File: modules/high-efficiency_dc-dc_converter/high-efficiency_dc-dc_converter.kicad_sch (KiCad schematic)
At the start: 13 parts

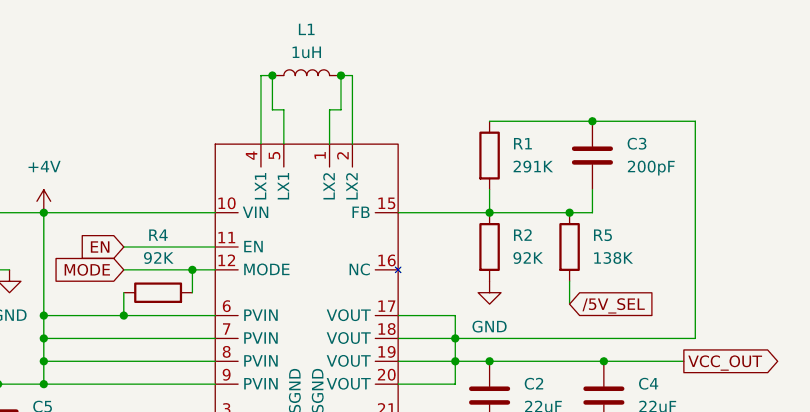
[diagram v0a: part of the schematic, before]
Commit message: Adding more mouser parts to schematics
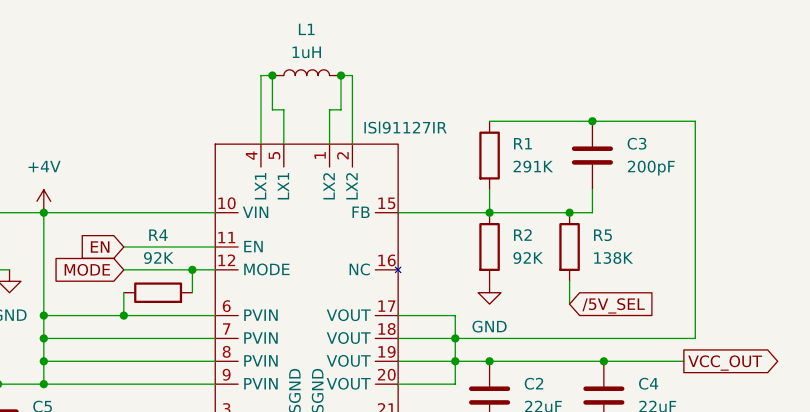
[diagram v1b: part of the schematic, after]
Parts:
- R2, R4: Mft. PN (none) -> RN73H1JTTD9202B25; Mouser (none) -> https://eu.mouser.com/ProductDetail/KOA-Speer/RN73H1JTTD920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; Mouser PN (none) -> 660-RN73H1JTD9202B25
- U1: value ~ -> ISl91127IR; Mft. PN (none) -> ISL91127IRAZ-T7A; Mouser (none) -> https://eu.mouser.com/ProductDetail/Renesas-Intersil/ISL911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; Mouser PN (none) -> 968-ISL91127IRAZ-T

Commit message: Updating parts
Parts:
- C1, C5: DigiKey (none) -> https://www.digikey.com.au/en/products/detail/samsung-elect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; Mft. PN (none) -> CL21A106KOQNNNG; Mouser (none) -> https://hr.mouser.com/ProductDetail/Samsung-Electro-Mechani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; Mouser PN (none) -> 187-CL21A106KOQNNNG
- C2, C4: DigiKey (none) -> https://www.digikey.com.au/en/products/detail/samsung-elect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; Mft. PN (none) -> CL21A226KOQNNNG; Mouser (none) -> https://hr.mouser.com/ProductDetail/Samsung-Electro-Mechani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; Mouser PN (none) -> 187-CL21A226KOQNNNG
- C3: DigiKey (none) -> https://www.digikey.com.au/en/products/detail/yageo/CC0805J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; Mft. PN (none) -> CC0805JRNPO9BN201; Mouser (none) -> 603-CC805JRNPO9BN201; Mouser PN (none) -> https://hr.mouser.com/ProductDetail/YAGEO/CC0805JRNPO9BN201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
- L1: DigiKey (none) -> https://www.digikey.com.au/en/products/detail/koa-speer-ele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; Mft. PN (none) -> DFE252012P-1R0M=P2; Mouser (none) -> https://hr.mouser.com/ProductDetail/Murata-Electronics/DFE2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; Mouser PN (none) -> 81-DFE252012P-1R0MP2
- R1: DigiKey (none) -> https://www.digikey.com/en/products/detail/koa-speer-electr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; Mft. PN (none) -> RN73R1JTTD2913F100
- R2, R4: DigiKey (none) -> https://www.digikey.com.au/en/products/detail/yageo/RC0603F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; Mft. PN RN73H1JTTD9202B25 -> RC0603FR-0791KL; Mouser https://eu.mouser.com/ProductDetail/KOA-Speer/RN73H1JTTD920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 -> https://hr.mouser.com/ProductDetail/YAGEO/RC0603FR-0791KL?q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; Mouser PN 660-RN73H1JTD9202B25 -> 603-RC0603FR-0791KL
- R5: DigiKey (none) -> https://www.digikey.com.au/en/products/detail/koa-speer-ele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; Mft. PN (none) -> RK73H1JTTD1403F; Mouser (none) -> https://eu.mouser.com/ProductDetail/KOA-Speer/RK73H1JTTD140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; Mouser PN (none) -> 660-RK73H1JTTD1403F
- U1: DigiKey (none) -> https://www.digikey.com/en/products/detail/renesas-electron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
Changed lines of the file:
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@@
 			)
 		)
-		(property "Mft. PN" ""
+		(property "Mft. PN" "RK73H1JTTD1403F"
 			(at 101.6 62.23 0)
 			(effects
@@
 			)
 		)
-		(property "Mouser" ""
+		(property "Mouser" "https://eu.mouser.com/ProductDetail/KOA-Speer/RK73H1JTTD1403F?qs=XOvILOgadXaHJrsLzSCu9w%3D%3D"
 			(at 101.6 62.23 0)
 			(effects
@@
 			)
 		)
-		(property "Mouser PN" ""
+		(property "Mouser PN" "660-RK73H1JTTD1403F"
+			(at 101.6 62.23 0)
+			(effects
+				(font
+					(size 1.27 1.27)
+				)
+				(hide yes)
+			)
+		)
+		(property "DigiKey" "https://www.digikey.com.au/en/products/detail/koa-speer-electronics-inc/RK73H1JTTD1403F/9845164"
 			(at 101.6 62.23 0)
 			(effects
@@
 			)
 		)
-		(property "Mft. PN" ""
+		(property "Mft. PN" "RN73R1JTTD2913F100"
 			(at 92.71 52.07 0)
 			(effects
@@
 		)
 		(property "Mouser PN" ""
+			(at 92.71 52.07 0)
+			(effects
+				(font
+					(size 1.27 1.27)
+				)
+				(hide yes)
+			)
+		)
+		(property "DigiKey" "https://www.digikey.com/en/products/detail/koa-speer-electronics-inc/RN73R1JTTD2913F100/10014619?s=N4IgTCBcDaIEoDkDsBmOBGAUgFWwETAE50UAxdABgpAF0BfIA"
 			(at 92.71 52.07 0)
 			(effects
@@
 			)
 		)
+		(property "DigiKey" "https://www.digikey.com/en/products/detail/renesas-electronics-corporation/ISL91127IRAZ-T7A/6163917"
+			(at 72.39 67.31 0)
+			(effects
+				(font
+					(size 1.27 1.27)
+				)
+				(hide yes)
+			)
+		)
 		(pin "5"
 		)
@@
 			)
 		)
-		(property "Mft. PN" "RN73H1JTTD9202B25"
+		(property "Mft. PN" "RC0603FR-0791KL"
 			(at 92.71 62.23 0)
 			(effects
@@
 			)
 		)
-		(property "Mouser" "https://eu.mouser.com/ProductDetail/KOA-Speer/RN73H1JTTD9202B25?qs=pJKkPLTLvBhLL59WGnN8iw%3D%3D"
+		(property "Mouser" "https://hr.mouser.com/ProductDetail/YAGEO/RC0603FR-0791KL?qs=EiqXWrxQq62Zxx9xQZom2g%3D%3D"
 			(at 92.71 62.23 0)
 			(effects
@@
 			)
 		)
-		(property "Mouser PN" " 660-RN73H1JTD9202B25"
+		(property "Mouser PN" "603-RC0603FR-0791KL"
+			(at 92.71 62.23 0)
+			(effects
+				(font
+					(size 1.27 1.27)
+				)
+				(hide yes)
+			)
+		)
+		(property "DigiKey" "https://www.digikey.com.au/en/products/detail/yageo/RC0603FR-0791KL/727428"
 			(at 92.71 62.23 0)
 			(effects
@@
 			)
 		)
-		(property "Mft. PN" "RN73H1JTTD9202B25"
+		(property "Mft. PN" "RC0603FR-0791KL"
 			(at 55.88 67.31 0)
 			(effects
@@
 			)
 		)
-		(property "Mouser" "https://eu.mouser.com/ProductDetail/KOA-Speer/RN73H1JTTD9202B25?qs=pJKkPLTLvBhLL59WGnN8iw%3D%3D"
+		(property "Mouser" "https://hr.mouser.com/ProductDetail/YAGEO/RC0603FR-0791KL?qs=EiqXWrxQq62Zxx9xQZom2g%3D%3D"
 			(at 55.88 67.31 0)
 			(effects
@@
 			)
 		)
-		(property "Mouser PN" " 660-RN73H1JTD9202B25"
+		(property "Mouser PN" "603-RC0603FR-0791KL"
+			(at 55.88 67.31 0)
+			(effects
+				(font
+					(size 1.27 1.27)
+				)
+				(hide yes)
+			)
+		)
+		(property "DigiKey" "https://www.digikey.com.au/en/products/detail/yageo/RC0603FR-0791KL/727428"
 			(at 55.88 67.31 0)
 			(effects
@@
 			)
 		)
-		(property "Mft. PN" ""
+		(property "Mft. PN" "CL21A106KOQNNNG"
 			(at 31.75 81.28 0)
 			(effects
@@
 			)
 		)
-		(property "Mouser" ""
+		(property "Mouser" "https://hr.mouser.com/ProductDetail/Samsung-Electro-Mechanics/CL21A106KOQNNNG?qs=hqM3L16%252BxlcMWI7QbqH0LA%3D%3D"
 			(at 31.75 81.28 0)
 			(effects
@@
 			)
 		)
-		(property "Mouser PN" ""
+		(property "Mouser PN" "187-CL21A106KOQNNNG"
+			(at 31.75 81.28 0)
+			(effects
+				(font
+					(size 1.27 1.27)
+				)
+				(hide yes)
+			)
+		)
+		(property "DigiKey" "https://www.digikey.com.au/en/products/detail/samsung-electro-mechanics/CL21A106KOQNNNG/3894417"
 			(at 31.75 81.28 0)
 			(effects
@@
 			)
 		)
-		(property "Mft. PN" ""
+		(property "Mft. PN" "CC0805JRNPO9BN201"
 			(at 104.14 52.07 0)
 			(effects
@@
 			)
 		)
-		(property "Mouser" ""
+		(property "Mouser" "603-CC805JRNPO9BN201"
 			(at 104.14 52.07 0)
 			(effects
@@
 			)
 		)
-		(property "Mouser PN" ""
+		(property "Mouser PN" "https://hr.mouser.com/ProductDetail/YAGEO/CC0805JRNPO9BN201?qs=57cj7OiSijkQwP0oHDWT0Q%3D%3D"
+			(at 104.14 52.07 0)
+			(effects
+				(font
+					(size 1.27 1.27)
+				)
+				(hide yes)
+			)
+		)
+		(property "DigiKey" "https://www.digikey.com.au/en/products/detail/yageo/CC0805JRNPO9BN201/5884041"
 			(at 104.14 52.07 0)
 			(effects
@@
 			)
 		)
+		(property "DigiKey" ""
+			(at 62.23 99.06 0)
+			(effects
+				(font
+					(size 1.27 1.27)
+				)
+				(hide yes)
+			)
+		)
 		(pin "1"
 		)
@@
 			)
 		)
-		(property "Mft. PN" ""
+		(property "Mft. PN" "CL21A106KOQNNNG"
 			(at 38.1 81.28 0)
 			(effects
@@
 			)
 		)
-		(property "Mouser" ""
+		(property "Mouser" "https://hr.mouser.com/ProductDetail/Samsung-Electro-Mechanics/CL21A106KOQNNNG?qs=hqM3L16%252BxlcMWI7QbqH0LA%3D%3D"
 			(at 38.1 81.28 0)
 			(effects
@@
 			)
 		)
-		(property "Mouser PN" ""
+		(property "Mouser PN" "187-CL21A106KOQNNNG"
+			(at 38.1 81.28 0)
+			(effects
+				(font
+					(size 1.27 1.27)
+				)
+				(hide yes)
+			)
+		)
+		(property "DigiKey" "https://www.digikey.com.au/en/products/detail/samsung-electro-mechanics/CL21A106KOQNNNG/3894417"
 			(at 38.1 81.28 0)
 			(effects
@@
 			)
 		)
+		(property "DigiKey" ""
+			(at 113.03 111.76 0)
+			(effects
+				(font
+					(size 1.27 1.27)
+				)
+				(hide yes)
+			)
+		)
 		(pin "13"
 		)
@@
 			)
 		)
-		(property "Mft. PN" ""
+		(property "Mft. PN" "CL21A226KOQNNNG"
 			(at 92.71 78.74 0)
 			(effects
@@
 			)
 		)
-		(property "Mouser" ""
+		(property "Mouser" "https://hr.mouser.com/ProductDetail/Samsung-Electro-Mechanics/CL21A226KOQNNNG?qs=y02iAgv9n63ATGKnSfEDrg%3D%3D"
 			(at 92.71 78.74 0)
 			(effects
@@
 			)
 		)
-		(property "Mouser PN" ""
+		(property "Mouser PN" "187-CL21A226KOQNNNG"
+			(at 92.71 78.74 0)
+			(effects
+				(font
+					(size 1.27 1.27)
+				)
+				(hide yes)
+			)
+		)
+		(property "DigiKey" "https://www.digikey.com.au/en/products/detail/samsung-electro-mechanics/CL21A226KOQNNNG/3894433?s=N4IgTCBcDaIMIBkwEYCCYwDYDSB5AigHLEDiIAugL5A"
 			(at 92.71 78.74 0)
 			(effects
@@
 			)
 		)
-		(property "Mft. PN" ""
+		(property "Mft. PN" "CL21A226KOQNNNG"
 			(at 105.41 78.74 0)
 			(effects
@@
 			)
 		)
-		(property "Mouser" ""
+		(property "Mouser" "https://hr.mouser.com/ProductDetail/Samsung-Electro-Mechanics/CL21A226KOQNNNG?qs=y02iAgv9n63ATGKnSfEDrg%3D%3D"
 			(at 105.41 78.74 0)
 			(effects
@@
 			)
 		)
-		(property "Mouser PN" ""
+		(property "Mouser PN" "187-CL21A226KOQNNNG"
+			(at 105.41 78.74 0)
+			(effects
+				(font
+					(size 1.27 1.27)
+				)
+				(hide yes)
+			)
+		)
+		(property "DigiKey" "https://www.digikey.com.au/en/products/detail/samsung-electro-mechanics/CL21A226KOQNNNG/3894433?s=N4IgTCBcDaIMIBkwEYCCYwDYDSB5AigHLEDiIAugL5A"
 			(at 105.41 78.74 0)
 			(effects
@@
 			)
 		)
-		(property "Mft. PN" ""
+		(property "Mft. PN" "DFE252012P-1R0M=P2"
 			(at 72.39 43.18 0)
 			(effects
@@
 			)
 		)
-		(property "Mouser" ""
+		(property "Mouser" "https://hr.mouser.com/ProductDetail/Murata-Electronics/DFE252012P-1R0M%3dP2?qs=KuGPmAKtFKUHla8Odvjl9w%3D%3D"
 			(at 72.39 43.18 0)
 			(effects
@@
 			)
 		)
-		(property "Mouser PN" ""
+		(property "Mouser PN" "81-DFE252012P-1R0MP2"
 			(at 72.39 43.18 0)
 			(effects
+				(font
+					(size 1.27 1.27)
+				)
+				(hide yes)
+			)
+		)
+		(property "DigiKey" "https://www.digikey.com.au/en/products/detail/koa-speer-electronics-inc/RN73R1JTTD2913F100/10014619"
+			(at 72.39 43.18 0)
+			(effects

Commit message: Updating high-efficiency_dc-dc_converter
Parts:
- M1: footprint MegaCastle:MegaCastle2x11-Module-I15.7x23.1-MA0780C-PANEL-NIBBLE -> MegaCastle:MegaCastle2x11-Module-I15.7x23.1-MA0780C-SPAREPAD
- U1: footprint QFN20:QFN50P400X400X90-21N -> MegaCastle:QFN50P400X400X90-21N
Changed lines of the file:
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@@
 (kicad_sch
-	(version 20231120)
+	(version 20250114)
 	(generator "eeschema")
-	(generator_version "8.0")
+	(generator_version "9.0")
 	(paper "A4")
 	(title_block
@@
 			)
 		)
-		(property "Footprint" "QFN20:QFN50P400X400X90-21N"
+		(property "Footprint" "MegaCastle:QFN50P400X400X90-21N"
 			(at 60.96 66.04 0)
 			(effects
@@
 			)
 		)
-		(property "Footprint" "MegaCastle:MegaCastle2x11-Module-I15.7x23.1-MA0780C-PANEL-NIBBLE"
+		(property "Footprint" "MegaCastle:MegaCastle2x11-Module-I15.7x23.1-MA0780C-SPAREPAD"
 			(at 113.03 132.08 0)
 			(effects
@@
 		)
 	)
+	(embedded_fonts no)
 )
